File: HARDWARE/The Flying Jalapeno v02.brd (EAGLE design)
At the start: 73.7 x 72.4 mm, 96 parts, among them Q2 MMBT2222A, Q3 NDP6020P, Q4 MMBT2222A, Q5 NDP6020P, Q6 BSS138, 200mA/50V, Q7 BSS138, 200mA/50V, U1 ATMEGA2560AU, U2 LM1117, U3 LM1117, U4 LM1117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

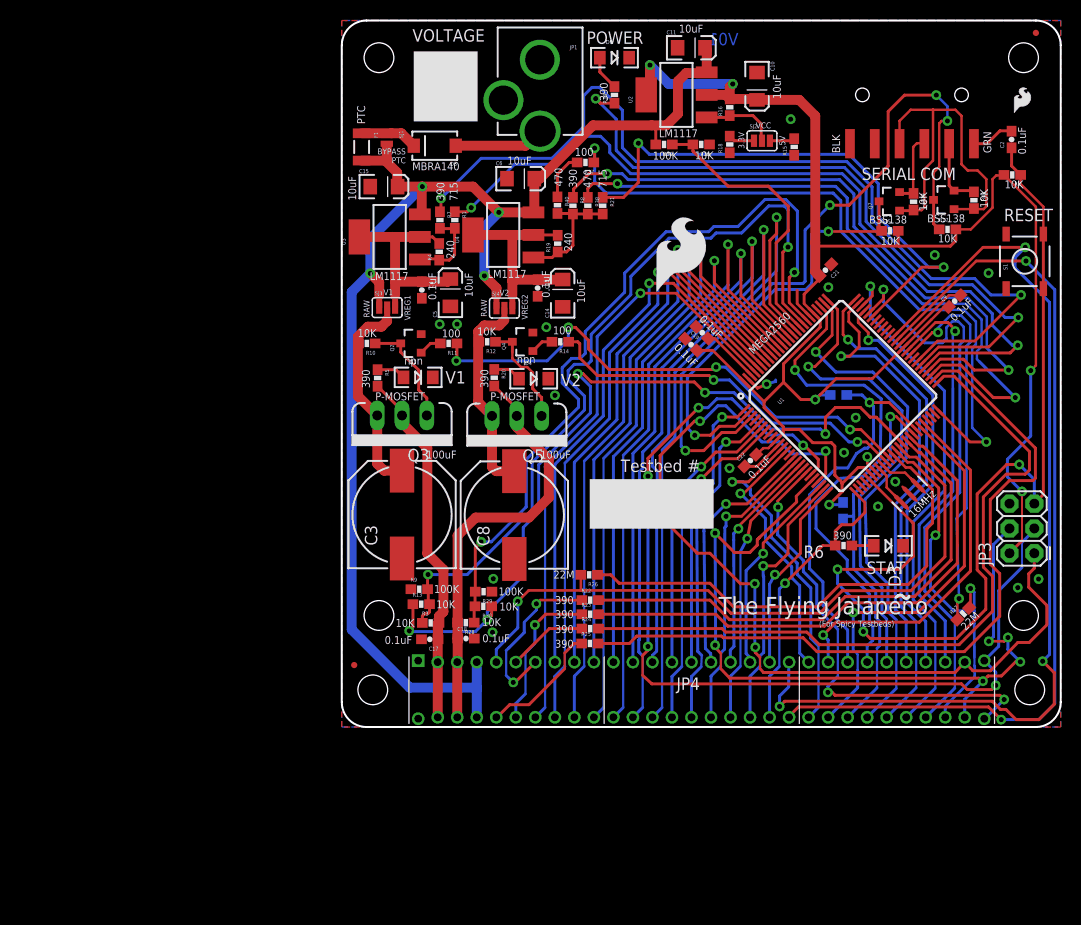
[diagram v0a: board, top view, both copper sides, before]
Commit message: added in PCA9306 for I2C - still not netted or routed
also added ignore for lock files
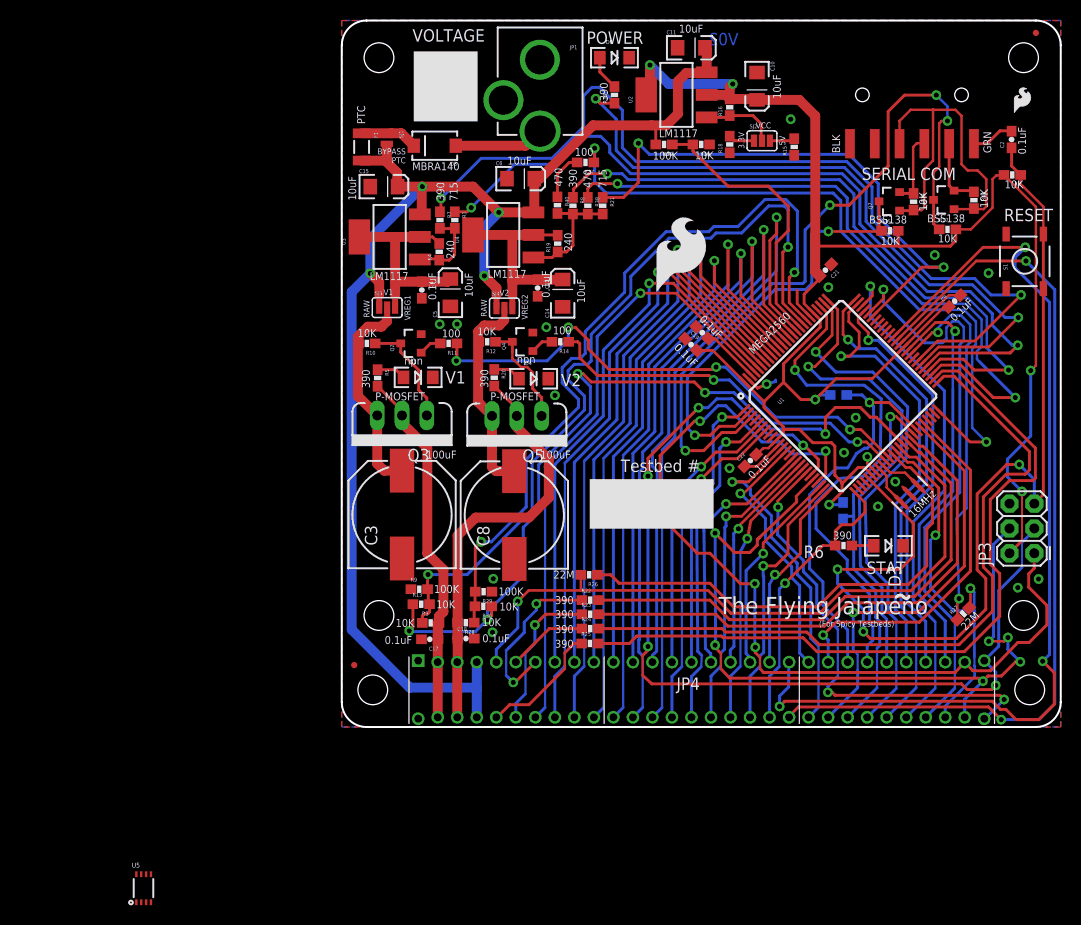
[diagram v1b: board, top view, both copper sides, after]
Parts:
- added U5: PCA9306, SparkFun-DigitalIC:PCA9306DC-1:1
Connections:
- new net EN: U5.8
- new net PMVCC: U5.1
- new net SCLB: U5.6
- new net SCLM: U5.2
- new net SDAB: U5.5
- new net SDAM: U5.3
- net GND: now also U5.4
- net VCC: now also U5.7
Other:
- board text added: "V02"
- board text removed: "V01"
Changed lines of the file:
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@@
 <?xml version="1.0" encoding="utf-8"?>
 <!DOCTYPE eagle SYSTEM "eagle.dtd">
-<eagle version="7.3.0">
+<eagle version="7.5.0">
 <drawing>
 <settings>
@@
 <layer number="113" name="IDFDebug" color="4" fill="1" visible="no" active="yes"/>
 <layer number="114" name="Badge_Outline" color="11" fill="1" visible="no" active="no"/>
+<layer number="115" name="ReferenceISLANDS" color="7" fill="1" visible="yes" active="yes"/>
 <layer number="116" name="Patch_BOT" color="9" fill="4" visible="no" active="yes"/>
 <layer number="118" name="Rect_Pads" color="7" fill="1" visible="no" active="yes"/>
@@
 <text x="51.054" y="58.801" size="0.8128" layer="21" font="vector" ratio="15" rot="R90">BLK</text>
 <text x="66.548" y="58.801" size="0.8128" layer="21" font="vector" ratio="15" rot="R90">GRN</text>
-<text x="40.64" y="69.85" size="1.27" layer="16" font="vector" ratio="15" rot="MR0">V01</text>
+<text x="40.64" y="69.85" size="1.27" layer="16" font="vector" ratio="15" rot="MR0">V02</text>
 <text x="7.239" y="70.231" size="1.27" layer="21" font="vector" ratio="15">VOLTAGE</text>
 <text x="2.2352" y="43.7388" size="0.6096" layer="21" font="vector" ratio="15" rot="R270">RAW</text>
@@
 </class>
 <class number="2" name="POWER" width="0.2032" drill="0">
+</class>
+<class number="10" name="12_mil" width="0.3048" drill="0.381">
+</class>
+<class number="11" name="15_mil" width="0.381" drill="0.381">
 </class>
 </classes>
@@
 </element>
 <element name="LOGO2" library="SparkFun-Aesthetics" package="SFE_LOGO_FLAME_.3" value="SFE_LOGO_FLAME.3_INCH" x="31.75" y="44.45"/>
+<element name="U5" library="SparkFun-DigitalIC" package="PCA9306DC-1:1" value="PCA9306" x="-20.32" y="-16.51">
+<attribute name="PROD_ID" value="IC-10023" x="-24.13" y="-10.16" size="1.778" layer="27" font="vector" ratio="15" display="off"/>
+</element>
 </elements>
 <signals>
@@
 <wire x1="54.707503125" y1="26.13985" x2="53.848" y2="26.999353125" width="0.254" layer="1"/>
 <wire x1="53.848" y1="26.999353125" x2="53.848" y2="27.686" width="0.254" layer="1"/>
+<contactref element="U5" pad="4"/>
+<wire x1="66.2686" y1="46.5074" x2="68.072" y2="50.5079" width="0" layer="19" extent="1-1"/>
+<wire x1="68.072" y1="44.9199" x2="66.2686" y2="46.5074" width="0" layer="19" extent="1-1"/>
+<wire x1="63.39494375" y1="44.24041875" x2="66.2686" y2="46.5074" width="0" layer="19" extent="1-1"/>
+<wire x1="60.7568" y1="48.3616" x2="62.201471875" y2="44.24041875" width="0" layer="19" extent="1-1"/>
+<wire x1="52.6542" y1="31.6992" x2="57.182378125" y2="39.221325" width="0" layer="19" extent="1-1"/>
+<wire x1="51.4604" y1="28.1178" x2="52.6542" y2="31.6992" width="0" layer="19" extent="1-1"/>
+<wire x1="53.848" y1="27.686" x2="51.4604" y2="28.1178" width="0" layer="19" extent="1-1"/>
+<wire x1="56.7182" y1="25.146" x2="54.707503125" y2="26.13985" width="0" layer="19" extent="1-1"/>
+<wire x1="57.448528125" y1="24.625228125" x2="56.7182" y2="25.146" width="0" layer="19" extent="1-1"/>
+<wire x1="54.9402" y1="22.606" x2="56.7182" y2="25.146" width="0" layer="19" extent="1-1"/>
+<wire x1="57.507" y1="18.5674" x2="54.9402" y2="22.606" width="0" layer="19" extent="1-1"/>
+<wire x1="44.808009375" y1="28.968275" x2="51.4604" y2="28.1178" width="0" layer="19" extent="1-1"/>
+<wire x1="39.7256" y1="26.5176" x2="41.25815625" y2="26.70395625" width="0" layer="19" extent="1-1"/>
+<wire x1="42.59001875" y1="34.7218" x2="44.808009375" y2="28.968275" width="0" layer="19" extent="1-1"/>
+<wire x1="47.989990625" y1="42.04975" x2="44.45" y2="35.56" width="0" layer="19" extent="1-16"/>
+<wire x1="49.8602" y1="45.0596" x2="46.6598" y2="44.7548" width="0" layer="19" extent="1-1"/>
+<wire x1="50.156440625" y1="47.413240625" x2="49.8602" y2="45.0596" width="0" layer="19" extent="1-1"/>
+<wire x1="36.330025" y1="41.012440625" x2="41.626028125" y2="35.685790625" width="0" layer="19" extent="1-1"/>
+<wire x1="35.181659375" y1="39.78861875" x2="36.330025" y2="41.012440625" width="0" layer="19" extent="1-1"/>
+<wire x1="68.4149" y1="22.8854" x2="58.88536875" y2="23.1883875" width="0" layer="19" extent="1-1"/>
+<wire x1="71.3994" y1="15.1638" x2="68.4149" y2="22.8854" width="0" layer="19" extent="1-1"/>
+<wire x1="69.2658" y1="14.2748" x2="71.3994" y2="15.1638" width="0" layer="19" extent="1-1"/>
+<wire x1="46.355" y1="58.586" x2="50.156440625" y2="47.413240625" width="0" layer="19" extent="1-1"/>
+<wire x1="45.9994" y1="62.2808" x2="46.355" y2="58.586" width="0" layer="19" extent="1-1"/>
+<wire x1="52.07" y1="59.77" x2="46.355" y2="58.586" width="0" layer="19" extent="1-1"/>
+<wire x1="54.61" y1="59.77" x2="52.07" y2="59.77" width="0" layer="19" extent="1-1"/>
+<wire x1="42.545" y1="67.059" x2="45.9994" y2="62.2808" width="0" layer="19" extent="1-1"/>
+<wire x1="39.751" y1="58.84" x2="46.355" y2="58.586" width="0" layer="19" extent="1-1"/>
+<wire x1="37.68" y1="59.69" x2="39.751" y2="58.84" width="0" layer="19" extent="1-1"/>
+<wire x1="34.414" y1="69.596" x2="42.545" y2="67.059" width="0" layer="19" extent="1-1"/>
+<wire x1="29.44" y1="68.58" x2="34.414" y2="69.596" width="0" layer="19" extent="1-1"/>
+<wire x1="20.2946" y1="68.373" x2="29.44" y2="68.58" width="0" layer="19" extent="1-1"/>
+<wire x1="16.5584" y1="64.23" x2="20.2946" y2="68.373" width="0" layer="19" extent="1-1"/>
+<wire x1="16.9261" y1="56.1848" x2="16.5584" y2="64.23" width="0" layer="19" extent="1-1"/>
+<wire x1="20.066" y1="44.1334" x2="16.9261" y2="56.1848" width="0" layer="19" extent="1-1"/>
+<wire x1="22.6314" y1="43.05" x2="20.066" y2="44.1334" width="0" layer="19" extent="1-1"/>
+<wire x1="20.955" y1="40.9702" x2="22.6314" y2="43.05" width="0" layer="19" extent="1-1"/>
+<wire x1="19.5801" y1="40.4216" x2="20.955" y2="40.9702" width="0" layer="19" extent="1-1"/>
+<wire x1="21.1596" y1="35.687" x2="19.5801" y2="40.4216" width="0" layer="19" extent="1-1"/>
+<wire x1="21.844" y1="33.9852" x2="21.1596" y2="35.687" width="0" layer="19" extent="1-1"/>
+<wire x1="11.811" y1="41.275" x2="19.5801" y2="40.4216" width="0" layer="19" extent="1-1"/>
+<wire x1="10.033" y1="41.275" x2="11.811" y2="41.275" width="0" layer="19" extent="1-1"/>
+<wire x1="11.1252" y1="43.1008" x2="11.811" y2="41.275" width="0" layer="19" extent="1-1"/>
+<wire x1="8.1374" y1="40.2565" x2="10.033" y2="41.275" width="0" layer="19" extent="1-1"/>
+<wire x1="8.2042" y1="43.9302" x2="11.1252" y2="43.1008" width="0" layer="19" extent="1-1"/>
+<wire x1="9.3232" y1="35.8267" x2="8.1374" y2="40.2565" width="0" layer="19" extent="1-1"/>
+<wire x1="2.918" y1="55.372" x2="8.2042" y2="43.9302" width="0" layer="19" extent="1-1"/>
+<wire x1="17.6784" y1="17.217" x2="21.844" y2="33.9852" width="0" layer="19" extent="1-1"/>
+<wire x1="15.5194" y1="15.1892" x2="17.6784" y2="17.217" width="0" layer="19" extent="1-1"/>
+<wire x1="15.3788" y1="13.8684" x2="15.5194" y2="15.1892" width="0" layer="19" extent="1-1"/>
+<wire x1="15.4432" y1="9.7028" x2="15.3788" y2="13.8684" width="0" layer="19" extent="1-1"/>
+<wire x1="13.5754" y1="9.0678" x2="15.4432" y2="9.7028" width="0" layer="19" extent="1-1"/>
+<wire x1="8.167" y1="8.9916" x2="13.5754" y2="9.0678" width="0" layer="19" extent="1-1"/>
+<wire x1="7.83" y1="6.8" x2="8.167" y2="8.9916" width="0" layer="19" extent="1-1"/>
+<wire x1="7.0875" y1="14.1224" x2="8.167" y2="8.9916" width="0" layer="19" extent="1-1"/>
+<wire x1="6.1722" y1="17.2678" x2="7.0875" y2="14.1224" width="0" layer="19" extent="1-1"/>
+<wire x1="7.83" y1="0.85" x2="7.83" y2="6.8" width="0" layer="19" extent="1-1"/>
+<wire x1="-19.55" y1="-17.9562" x2="7.83" y2="0.85" width="0" layer="19" extent="1-1"/>
 </signal>
 <signal name="AREF">
@@
 <wire x1="50.6603" y1="35.6997" x2="48.514" y2="33.5534" width="0.2794" layer="1"/>
 <wire x1="48.95435625" y1="46.21115625" x2="48.514" y2="46.6515125" width="1.016" layer="1"/>
+<contactref element="U5" pad="7"/>
+<wire x1="-20.55" y1="-15.0792" x2="42.460240625" y2="27.906040625" width="0" layer="19" extent="1-1"/>
 </signal>
 <signal name="RAW" class="1">
@@
 <wire x1="23.3045" y1="57.8485" x2="24.1182" y2="57.8485" width="0.3048" layer="1"/>
 </signal>
+<signal name="SCLM" class="10">
+<contactref element="U5" pad="2"/>
+</signal>
+<signal name="EN" class="10">
+<contactref element="U5" pad="8"/>
+</signal>
+<signal name="SCLB" class="10">
+<contactref element="U5" pad="6"/>
+</signal>
+<signal name="SDAM" class="10">
+<contactref element="U5" pad="3"/>
+</signal>
+<signal name="SDAB" class="10">
+<contactref element="U5" pad="5"/>
+</signal>
+<signal name="PMVCC" class="10">
+<contactref element="U5" pad="1"/>
+</signal>
 </signals>

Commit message: Placed/routed the PCA9306 into the design
Still some silk labeling to do, and check that GND pours are as good as
they can flow.
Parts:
- removed R31, R32: DNP, SparkFun-Resistors:0603-RES
- added C12: 10uF, SparkFun-Capacitors:0603-POL
- added C20: 10nF, SparkFun-Capacitors:0603
- added C7: 0.1uF, SparkFun-Capacitors:0603-CAP
- added TP1: TEST-POINT3, SparkFun-Passives:PAD.03X.03
- added U6: 3.3V MIC5205, SparkFun-PowerIC:SOT23-5
- moved U5 95.2 mm to (63.8, 28.2), turned to 90 degrees
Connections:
- removed net EN: U5.8
- removed net PMVCC: U5.1
- removed net SCL: JP4.53, R32.1, U1.43
- removed net SCLB: U5.6
- removed net SCLM: U5.2
- removed net SDA: JP4.23, R31.1, U1.44
- removed net SDAB: U5.5
- removed net SDAM: U5.3
- new net 3.3V: C12.A, C7.1, TP1.P$1, U5.1, U6.5
- new net EN_I2C: U1.47, U5.8
- new net N$2: U1.44, U5.5
- new net N$27: U1.43, U5.6
- new net N$28: C20.1, U6.4
- new net SCL1: JP4.53, U5.2
- new net SDA1: JP4.23, U5.3
- net GND: now also C12.K, C20.2, C7.2, U6.2
- net RAW: now also U6.1, U6.3
- net VCC: no longer R31.2, R32.2
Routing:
- net 3.3V: track 0.00 -> 81.9 mm, vias 0 -> 3
- net SCL1: track 0.00 -> 59.7 mm, vias 0 -> 1
- net SDA1: track 0.00 -> 49.4 mm, vias 0 -> 3
- net SDA: track 40.7 -> 0.00 mm, vias 1 -> 0
- net SCL: track 39.2 -> 0.00 mm, vias 1 -> 0
- net RAW: track 141.8 -> 156.8 mm, vias 4 -> 5
- net 37/V2_3.7V: track 69.4 -> 61.0 mm
- net EN_I2C: track 0.00 -> 6.30 mm, vias 0 -> 2
- net 36/V2_3.3V: track 67.6 -> 62.8 mm
- net 38/V2_4.2V: track 71.2 -> 66.5 mm
- net 35/V1_5V: track 83.9 -> 79.4 mm
- net N$27: track 0.00 -> 4.37 mm
- net 33/V1_3.3V: track 93.9 -> 89.6 mm
- net N$28: track 0.00 -> 4.09 mm
- net N$2: track 0.00 -> 3.96 mm
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
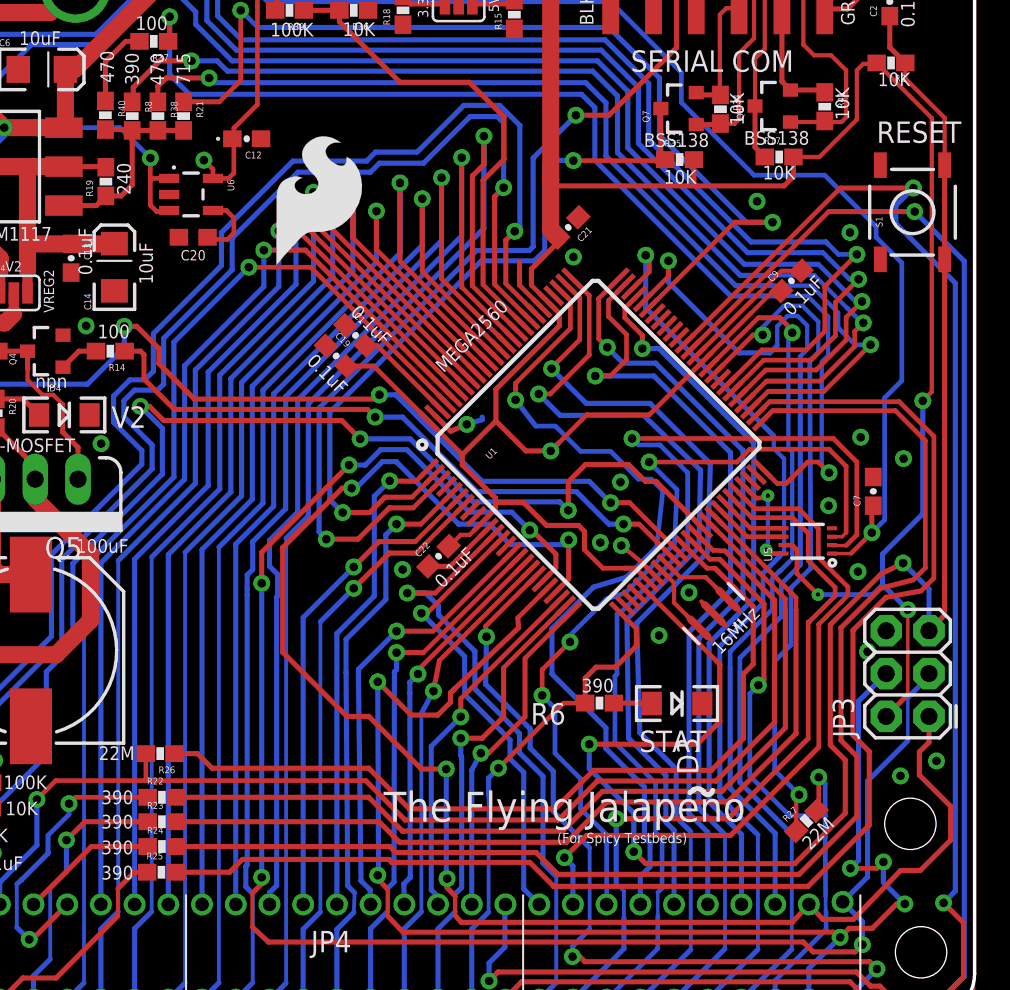
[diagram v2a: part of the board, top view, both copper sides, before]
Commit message: finished up routing and adjusted silk
Added/updated silk to:
Led resistors (stat and 4 others)- now are 1K
MIC5205 3.3V vreg
10uF pol cap
10nF bypass cap - near vreg
PCA9306
0.1uF cap near PCA9306
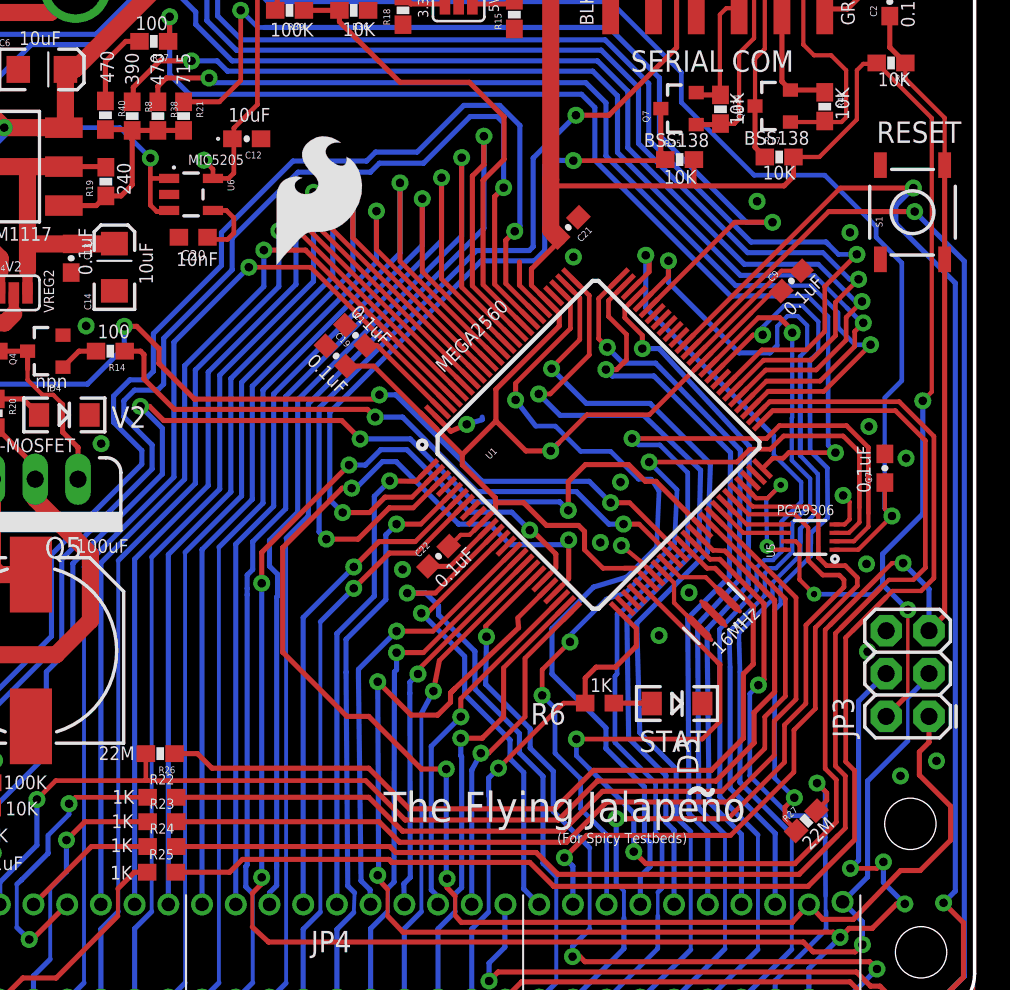
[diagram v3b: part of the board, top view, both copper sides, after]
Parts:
- R22, R23, R24, R25, R6: value 390 -> 1k; device SparkFun-Resistors:0603-RES -> SparkFun-Resistors:0603
- moved C7 1.53 mm to (68.3, 32.5)
- moved U5 0.27 mm to (63.9, 28.4)
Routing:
- net GND: track 22.2 -> 24.8 mm
- net SDA1: track 49.4 -> 51.5 mm
- net SCL1: track 59.7 -> 61.7 mm
- net 31/CAPRETURN2: track 40.4 -> 42.3 mm
- net EN_I2C: track 6.30 -> 8.08 mm
- net 38/V2_4.2V: track 66.5 -> 64.7 mm
- net TX1: track 40.8 -> 42.4 mm
- net D26: track 45.8 -> 44.5 mm
- net RESET: track 99.8 -> 101.0 mm
- net RX1: track 44.4 -> 45.6 mm
- net D27: track 53.9 -> 55.0 mm
- net D30: track 43.4 -> 44.3 mm
- net D29: track 60.2 -> 61.1 mm
- net 3.3V: track 81.9 -> 82.7 mm
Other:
- board text added: "10nF"
- board text added: "1K"
- board text added: "MIC5205"
- board text added: "PCA9306"
